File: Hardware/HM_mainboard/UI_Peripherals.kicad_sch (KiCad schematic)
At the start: 16 parts, among them J4 FC68125, U3 WE-TVS-824015043

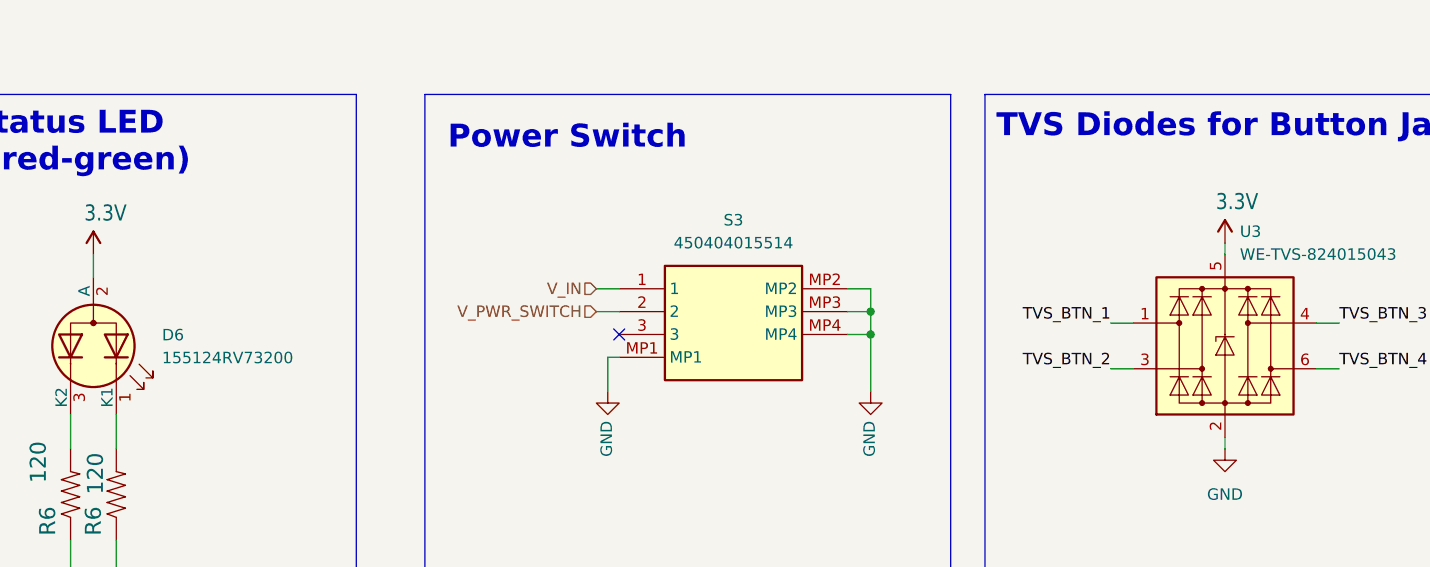
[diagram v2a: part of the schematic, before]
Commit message: Updated port connectors of microcontroller
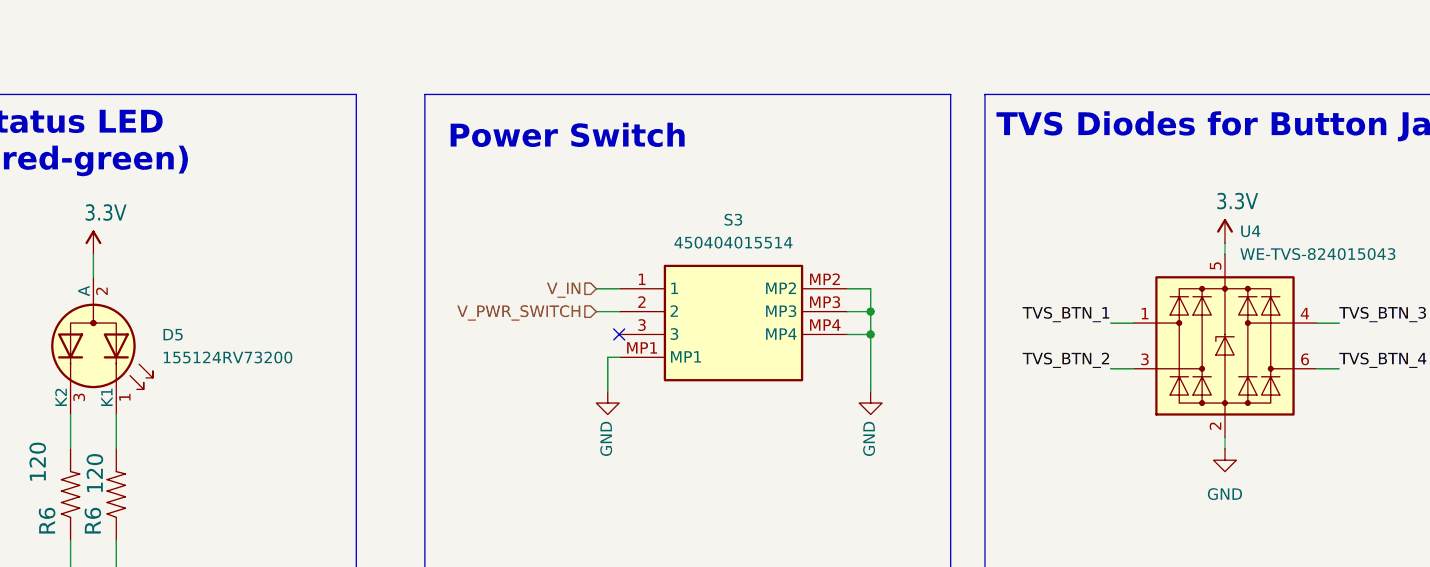
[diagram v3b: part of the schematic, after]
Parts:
- renumbered D6 to D5, U3 to U4
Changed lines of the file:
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@@
   (symbol (lib_id "Device:LED_Dual_KAK") (at 120.65 137.16 270) (unit 1)
     (in_bom yes) (on_board yes) (dnp no) (fields_autoplaced)
-    (property "Reference" "D6" (at 128.27 135.9535 90)
+    (property "Reference" "D5" (at 128.27 135.9535 90)
       (effects (font (size 1.27 1.27)) (justify left))
     )
@@
       (project "HM_mainboard"
         (path "/54a6df43-5475-46a2-9916-8b0260700d4c/137c5701-d01e-40ce-919d-b371cfda41da"
-          (reference "D6") (unit 1)
+          (reference "D5") (unit 1)
         )
       )
@@
         )
         (path "/54a6df43-5475-46a2-9916-8b0260700d4c/137c5701-d01e-40ce-919d-b371cfda41da"
-          (reference "#PWR07") (unit 1)
+          (reference "#PWR023") (unit 1)
         )
       )
@@
   (symbol (lib_id "Power_Protection:WE-TVS-824015043") (at 246.38 137.16 0) (unit 1)
     (in_bom yes) (on_board yes) (dnp no) (fields_autoplaced)
-    (property "Reference" "U3" (at 248.0311 124.46 0)
+    (property "Reference" "U4" (at 248.0311 124.46 0)
       (effects (font (size 1.27 1.27)) (justify left))
     )
@@
       (project "HM_mainboard"
         (path "/54a6df43-5475-46a2-9916-8b0260700d4c/137c5701-d01e-40ce-919d-b371cfda41da"
-          (reference "U3") (unit 1)
+          (reference "U4") (unit 1)
         )
       )
@@
         )
         (path "/54a6df43-5475-46a2-9916-8b0260700d4c/137c5701-d01e-40ce-919d-b371cfda41da"
-          (reference "R6") (unit 1)
+          (reference "R11") (unit 1)
         )
       )
@@
         )
         (path "/54a6df43-5475-46a2-9916-8b0260700d4c/137c5701-d01e-40ce-919d-b371cfda41da"
-          (reference "J3") (unit 1)
+          (reference "J4") (unit 1)
         )
       )
@@
         )
         (path "/54a6df43-5475-46a2-9916-8b0260700d4c/137c5701-d01e-40ce-919d-b371cfda41da"
-          (reference "#PWR05") (unit 1)
+          (reference "#PWR021") (unit 1)
         )
       )
@@
         )
         (path "/54a6df43-5475-46a2-9916-8b0260700d4c/137c5701-d01e-40ce-919d-b371cfda41da"
-          (reference "R5") (unit 1)
+          (reference "R10") (unit 1)
         )
       )
@@
         )
         (path "/54a6df43-5475-46a2-9916-8b0260700d4c/137c5701-d01e-40ce-919d-b371cfda41da"
-          (reference "#PWR04") (unit 1)
+          (reference "#PWR020") (unit 1)
         )
       )
@@
         )
         (path "/54a6df43-5475-46a2-9916-8b0260700d4c/137c5701-d01e-40ce-919d-b371cfda41da"
-          (reference "#PWR03") (unit 1)
+          (reference "#PWR019") (unit 1)
         )
       )
@@
         )
         (path "/54a6df43-5475-46a2-9916-8b0260700d4c/137c5701-d01e-40ce-919d-b371cfda41da"
-          (reference "#PWR02") (unit 1)
+          (reference "#PWR018") (unit 1)
         )
       )
@@
         )
         (path "/54a6df43-5475-46a2-9916-8b0260700d4c/137c5701-d01e-40ce-919d-b371cfda41da"
-          (reference "#PWR01") (unit 1)
+          (reference "#PWR017") (unit 1)
         )
       )
@@
         )
         (path "/54a6df43-5475-46a2-9916-8b0260700d4c/137c5701-d01e-40ce-919d-b371cfda41da"
-          (reference "#PWR08") (unit 1)
+          (reference "#PWR024") (unit 1)
         )
       )
@@
         )
         (path "/54a6df43-5475-46a2-9916-8b0260700d4c/137c5701-d01e-40ce-919d-b371cfda41da"
-          (reference "#PWR014") (unit 1)
+          (reference "#PWR026") (unit 1)
         )
       )
@@
         )
         (path "/54a6df43-5475-46a2-9916-8b0260700d4c/137c5701-d01e-40ce-919d-b371cfda41da"
-          (reference "C14") (unit 1)
+          (reference "C8") (unit 1)
         )
       )
@@
         )
         (path "/54a6df43-5475-46a2-9916-8b0260700d4c/137c5701-d01e-40ce-919d-b371cfda41da"
-          (reference "#PWR013") (unit 1)
+          (reference "#PWR025") (unit 1)
         )
       )
@@
         )
         (path "/54a6df43-5475-46a2-9916-8b0260700d4c/137c5701-d01e-40ce-919d-b371cfda41da"
-          (reference "#SUPPLY010") (unit 1)
+          (reference "#SUPPLY013") (unit 1)
         )
       )
@@
         )
         (path "/54a6df43-5475-46a2-9916-8b0260700d4c/137c5701-d01e-40ce-919d-b371cfda41da"
-          (reference "C16") (unit 1)
+          (reference "C10") (unit 1)
         )
       )
@@
         )
         (path "/54a6df43-5475-46a2-9916-8b0260700d4c/137c5701-d01e-40ce-919d-b371cfda41da"
-          (reference "J4") (unit 1)
+          (reference "J5") (unit 1)
         )
       )
@@
         )
         (path "/54a6df43-5475-46a2-9916-8b0260700d4c/137c5701-d01e-40ce-919d-b371cfda41da"
-          (reference "J5") (unit 1)
+          (reference "J6") (unit 1)
         )
       )
@@
         )
         (path "/54a6df43-5475-46a2-9916-8b0260700d4c/137c5701-d01e-40ce-919d-b371cfda41da"
-          (reference "#PWR06") (unit 1)
+          (reference "#PWR022") (unit 1)
         )
       )
@@
         )
         (path "/54a6df43-5475-46a2-9916-8b0260700d4c/137c5701-d01e-40ce-919d-b371cfda41da"
-          (reference "#SUPPLY011") (unit 1)
+          (reference "#SUPPLY014") (unit 1)
         )
       )
@@
         )
         (path "/54a6df43-5475-46a2-9916-8b0260700d4c/137c5701-d01e-40ce-919d-b371cfda41da"
-          (reference "R11") (unit 1)
+          (reference "R9") (unit 1)
         )
       )
@@
         )
         (path "/54a6df43-5475-46a2-9916-8b0260700d4c/137c5701-d01e-40ce-919d-b371cfda41da"
-          (reference "#SUPPLY06") (unit 1)
+          (reference "#SUPPLY015") (unit 1)
         )
       )
@@
         )
         (path "/54a6df43-5475-46a2-9916-8b0260700d4c/137c5701-d01e-40ce-919d-b371cfda41da"
-          (reference "R8") (unit 1)
+          (reference "R12") (unit 1)
         )
       )
@@
         )
         (path "/54a6df43-5475-46a2-9916-8b0260700d4c/137c5701-d01e-40ce-919d-b371cfda41da"
-          (reference "C13") (unit 1)
+          (reference "C7") (unit 1)
         )
       )
@@
         )
         (path "/54a6df43-5475-46a2-9916-8b0260700d4c/137c5701-d01e-40ce-919d-b371cfda41da"
-          (reference "J2") (unit 1)
+          (reference "J3") (unit 1)
         )
       )
@@
         )
         (path "/54a6df43-5475-46a2-9916-8b0260700d4c/137c5701-d01e-40ce-919d-b371cfda41da"
-          (reference "#PWR015") (unit 1)
+          (reference "#PWR027") (unit 1)
         )
       )
@@
         )
         (path "/54a6df43-5475-46a2-9916-8b0260700d4c/137c5701-d01e-40ce-919d-b371cfda41da"
-          (reference "C15") (unit 1)
-        )
-      )
+          (reference "C9") (unit 1)
+        )
+      )

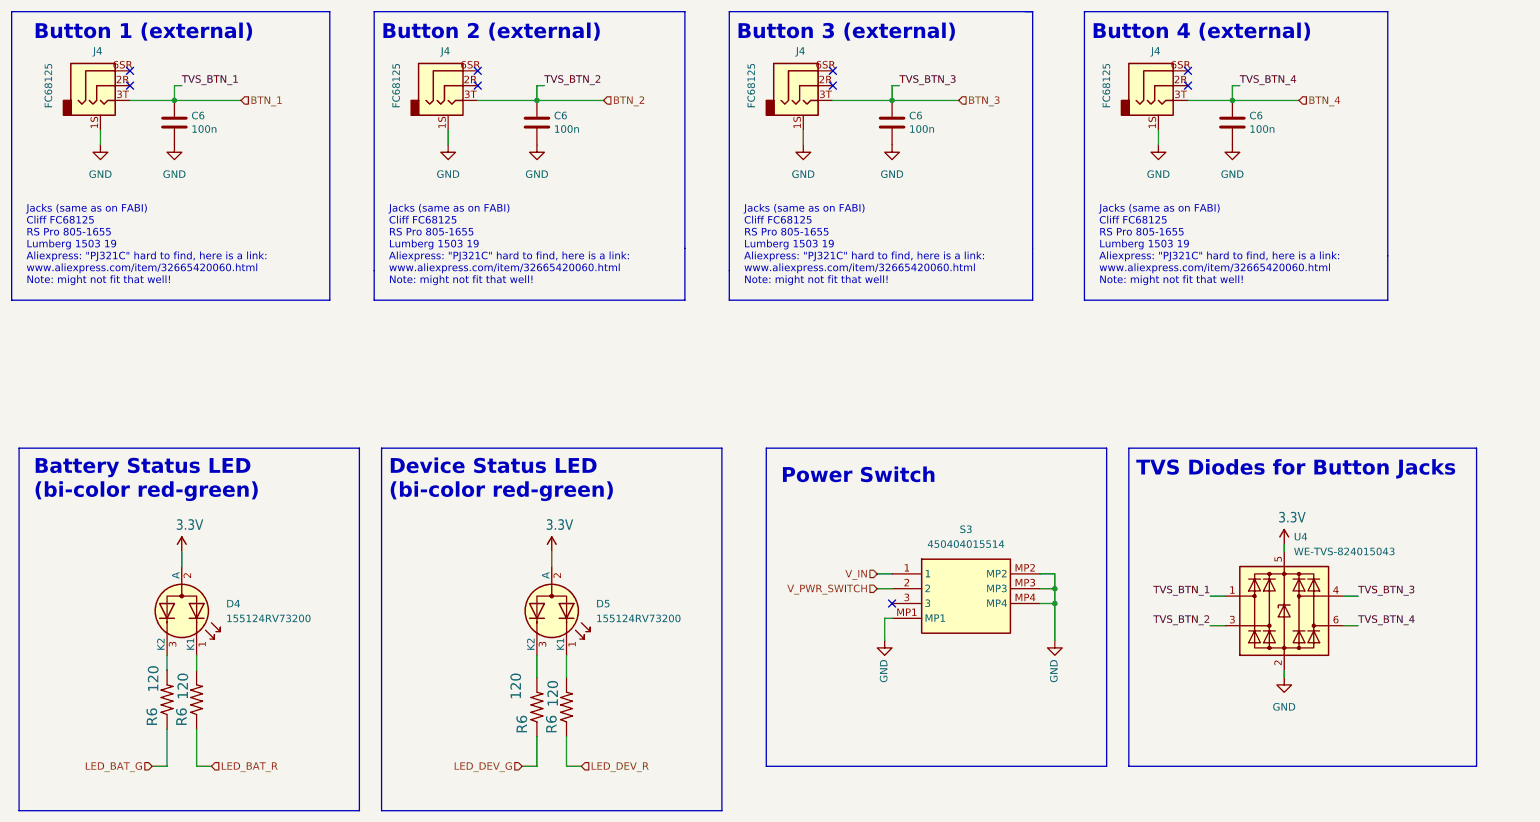
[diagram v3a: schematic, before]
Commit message: Added IMUs, updated some components
- Added 2 additonal IMUs:
     1) 6-Axis MC6470
     2) 9-Axis BNO55
- Replaced button jack connectors
- Replaced battery charging LED by a charging status measurement circuit
- Replaced caps for clock crystal
- Added stabalizing caps to uC Vcc
- Added UART pin header
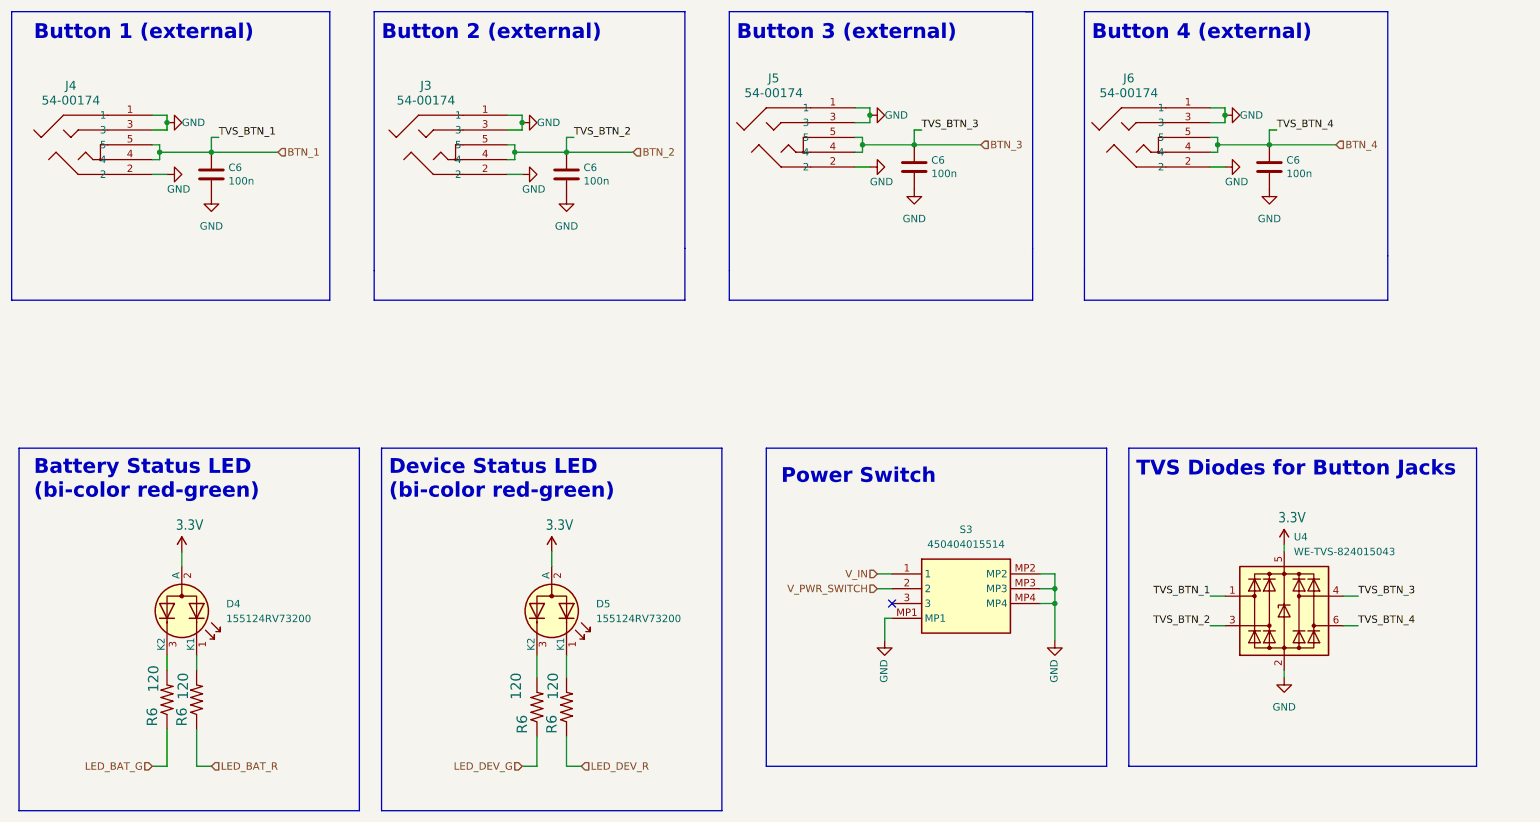
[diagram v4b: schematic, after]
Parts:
- removed J4 (x4): FC68125, HeadMouse:FC68125, symbol FC68125:AudioJack3_Ground
- added J3, J4, J5, J6: 54-00174, 54-00174_TEN, symbol HeadMouse:54-00174
- R6: footprint Resistor_SMD:R_0201_0603Metric_Pad0.64x0.40mm_HandSolder -> Resistor_SMD:R_0603_1608Metric_Pad0.98x0.95mm_HandSolder
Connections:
- net BTN_1: now also J4.4, J4.5
- net BTN_2: now also J3.4, J3.5
- net BTN_3: now also J5.4, J5.5
- net BTN_4: now also J6.4, J6.5
- net GND: now also J3.1, J3.2, J3.3, J4.1, J4.2, J4.3, J5.1, J5.2, J5.3, J6.1, J6.2, J6.3
- no-connect marks 9 -> 1
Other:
- note removed: "Jacks (same as on FABI) Cliff FC68125 RS Pro 805-1655 Lumberg 1503 19 Aliexpress: "PJ321C" hard to find, here is a link: www.aliexpress.com/item/32665420060.html Note: might not fit that well!"
- moved on the sheet: C6
